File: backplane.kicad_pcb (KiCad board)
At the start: 4 copper layers, 110 x 90 mm, 55 parts, among them J0 212520-1006, J1 SFMC-110-01-L-D, J2 SFMC-110-01-L-D, J3 SFMC-110-01-L-D, J5 XT60PW-F, Q1 SSM3K15AMFV,L3F, U1 SiC437BED-T1-GE3

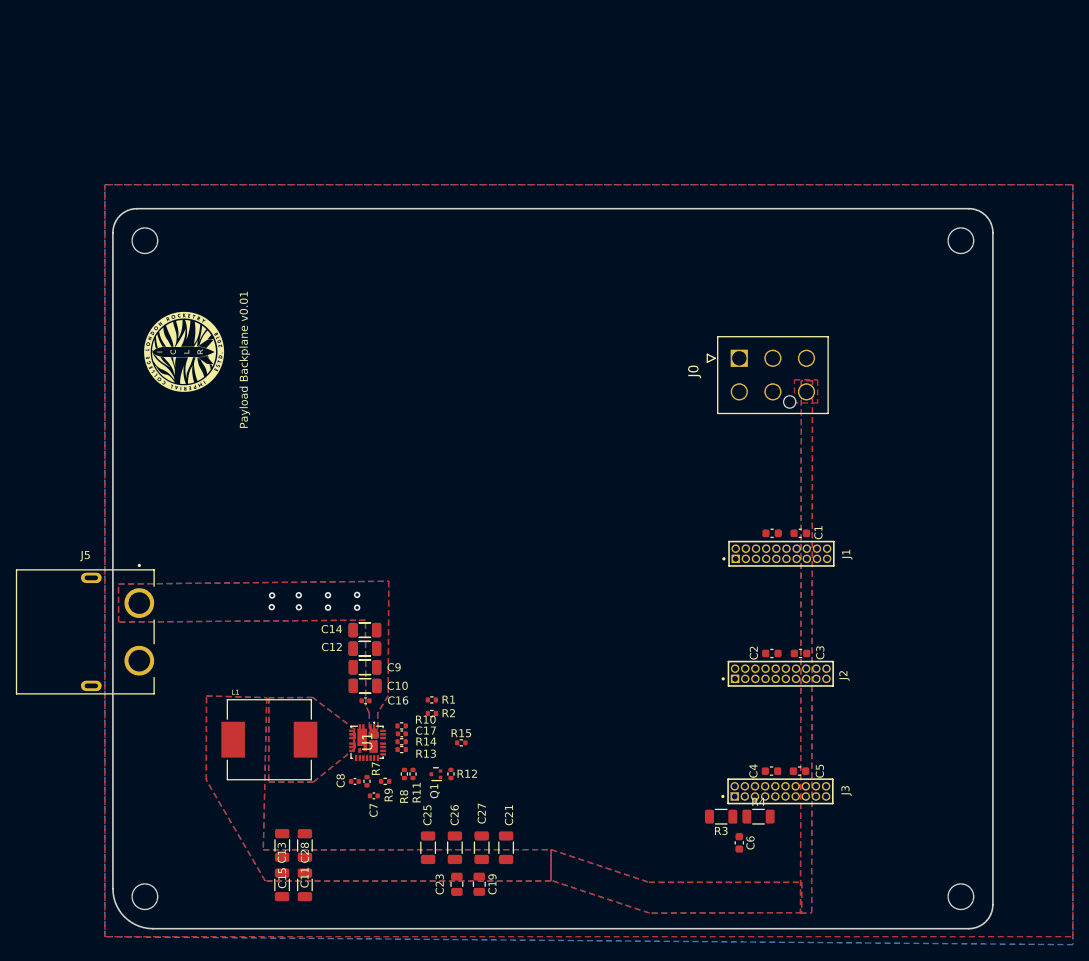
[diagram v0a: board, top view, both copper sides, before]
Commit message: Overhaul of design
Changed out the SFMC Oresat connectors for the 46010-0622 Molex; added the SC4215; reduced from 4 connectors to three connectors - no changes made to the footprint, changes only made to the schematic for checks
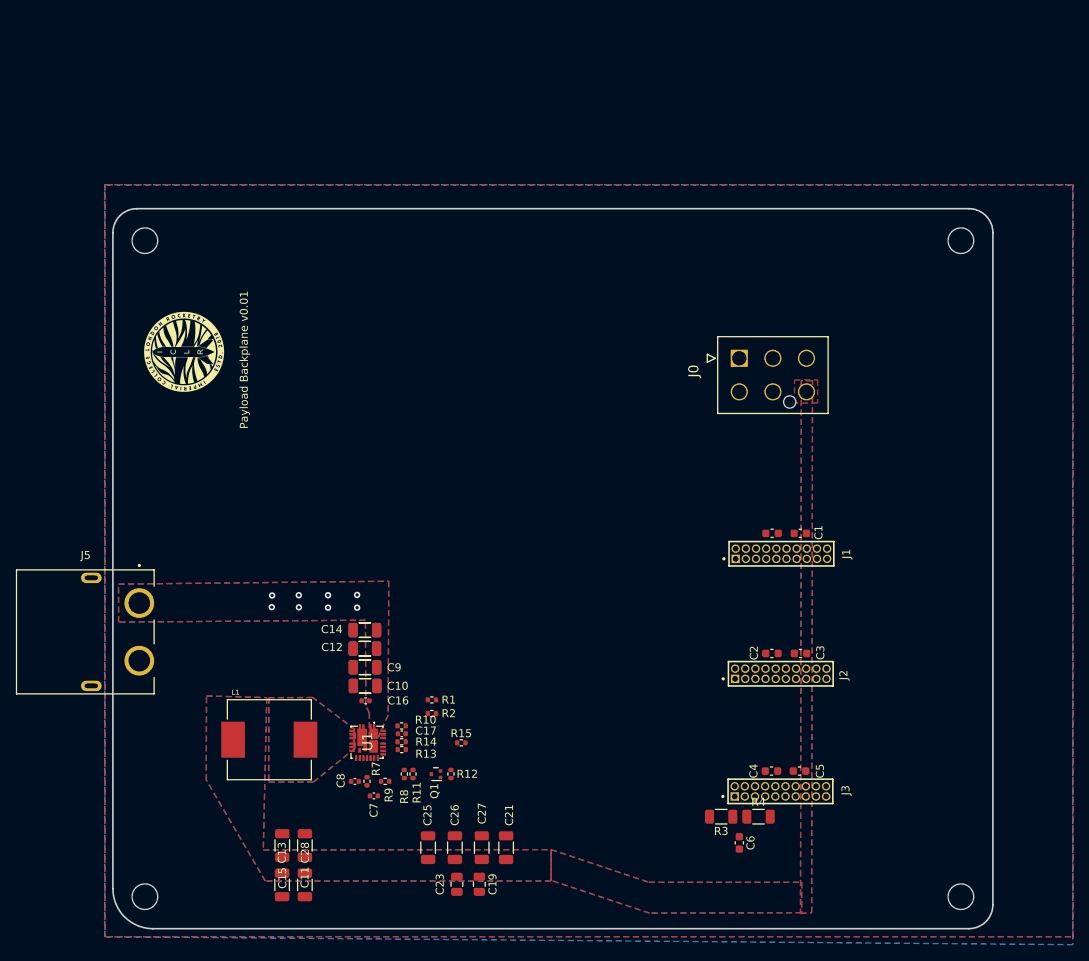
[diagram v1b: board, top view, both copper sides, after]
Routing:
- added copper zone on In2.Cu, net +3.3V
- removed copper zone on In2.Cu, net GND
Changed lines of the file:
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@@
   (via (at 113.89 106.32) (size 0.8) (drill 0.4) (layers "F.Cu" "B.Cu") (free) (net 11))
   (via (at 113.89 107.87) (size 0.8) (drill 0.4) (layers "F.Cu" "B.Cu") (free) (net 11))
-  (zone (net 2) (net_name "GND") (layer "F.Cu") (hatch edge 0.5)
+  (zone (net 0) (net_name "") (layer "F.Cu") (hatch edge 0.5)
+    (priority 6)
+    (connect_pads (clearance 0.254))
+    (min_thickness 0.25) (filled_areas_thickness no)
+    (fill yes (thermal_gap 0.5) (thermal_bridge_width 0.5) (island_removal_mode 1) (island_area_min 10))
+    (polygon
+      (pts
+        (xy 172.2 79.4)
+        (xy 175.1 79.4)
+        (xy 175.1 82.3)
+        (xy 172.2 82.3)
+      )
+    )
+  )
+  (zone (net 2) (net_name "GND") (layers "F.Cu" "In1.Cu" "B.Cu") (hatch edge 0.5)
     (priority 1)
-    (connect_pads (clearance 0.5))
+    (connect_pads yes (clearance 0.5))
     (min_thickness 0.25) (filled_areas_thickness no)
     (fill yes (thermal_gap 0.5) (thermal_bridge_width 0.5))
@@
         (xy 86 55)
         (xy 86 149)
-      )
-    )
-  )
-  (zone (net 0) (net_name "") (layer "F.Cu") (hatch edge 0.5)
-    (priority 6)
-    (connect_pads (clearance 0.254))
-    (min_thickness 0.25) (filled_areas_thickness no)
-    (fill (thermal_gap 0.5) (thermal_bridge_width 0.5) (island_removal_mode 1) (island_area_min 10))
-    (polygon
-      (pts
-        (xy 172.2 79.4)
-        (xy 175.1 79.4)
-        (xy 175.1 82.3)
-        (xy 172.2 82.3)
       )
     )
@@
         (xy 121.48 104.57)
         (xy 121.42 118.89)
-        (xy 120.1 121.01)
+        (xy 121.4 121.3)
         (xy 120.13 124.16)
       )
@@
     (connect_pads yes (clearance 0.254))
     (min_thickness 0.25) (filled_areas_thickness no)
-    (fill (thermal_gap 0.5) (thermal_bridge_width 0.5))
+    (fill yes (thermal_gap 0.5) (thermal_bridge_width 0.5))
     (polygon
       (pts
@@
     )
   )
-  (zone (net 2) (net_name "GND") (layer "In2.Cu") (hatch edge 0.5)
-    (priority 3)
-    (connect_pads (clearance 0.5))
+  (zone (net 12) (net_name "+3.3V") (layer "In2.Cu") (hatch edge 0.5)
+    (priority 1)
+    (connect_pads yes (clearance 0.5))
     (min_thickness 0.25) (filled_areas_thickness no)
     (fill yes (thermal_gap 0.5) (thermal_bridge_width 0.5))

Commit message: Configuring stuff
wires and zones added - will change to Si438 + add a switch at some point + some mistakes to still iron out
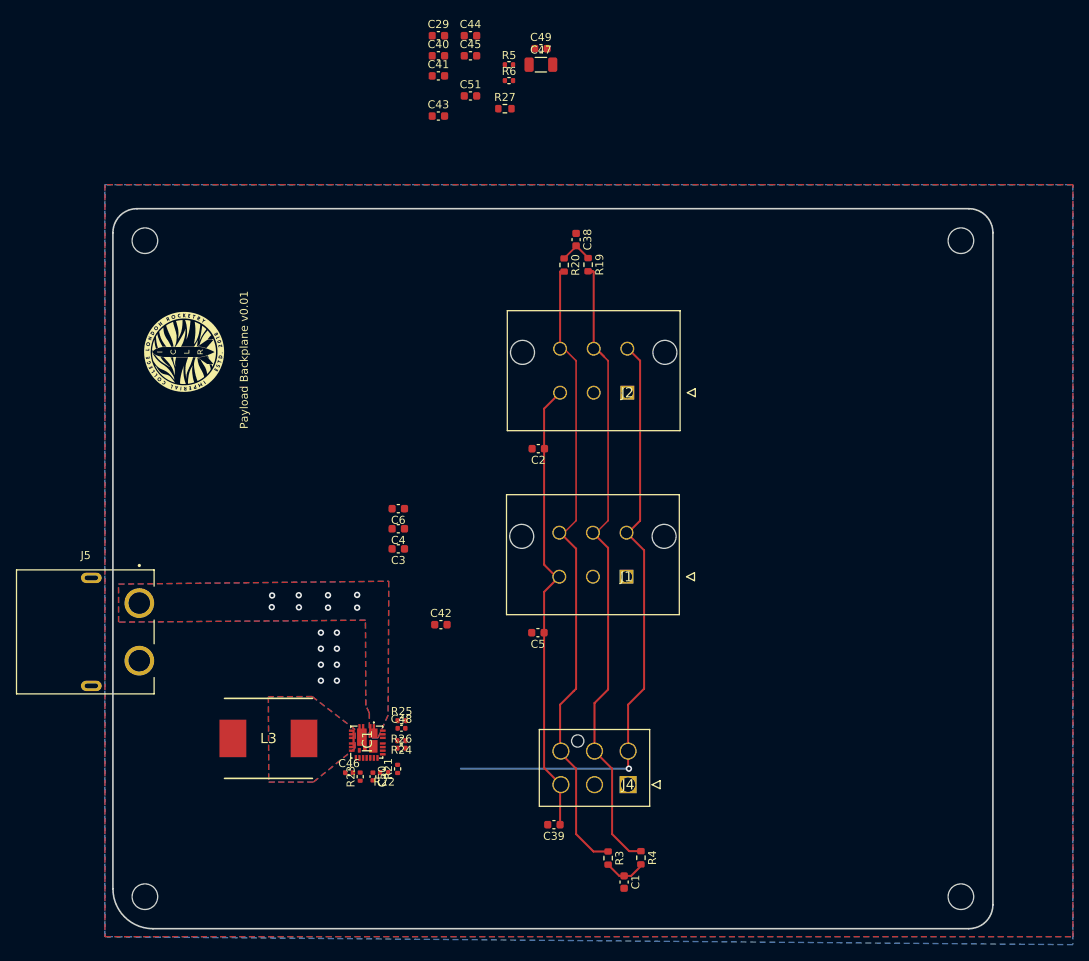
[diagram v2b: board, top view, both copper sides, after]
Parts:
- removed C10, C11, C13, C15, C28, C9: 47uF, Capacitor_SMD:C_1206_3216Metric
- removed C12, C14, C18, C20, C21, C22, C24, C25, C26, C27: DNP, Capacitor_SMD:C_1206_3216Metric
- removed C16: 100nF, Capacitor_SMD:C_0402_1005Metric
- removed C17: 0.1uF, Capacitor_SMD:C_0402_1005Metric
- removed C19, C23: DNP, Capacitor_SMD:C_0805_2012Metric
- removed C7: 1uF, Capacitor_SMD:C_0402_1005Metric
- removed C8: 4.7uF, Capacitor_SMD:C_0402_1005Metric
- removed J0: 212520-1006, Molex 212520-1006:212520-1006
- removed J3: SFMC-110-01-L-D, SFMC-110-01-L-D:SAMTEC_SFMC-110-01-L-D
- removed L1: 1.5uH, SPM10065VT_3R3M_D:IND_SPM10065VT-3R3M-D
- removed Q1: SSM3K15AMFV,L3F, Package_TO_SOT_SMD:SOT-723
- removed R1: 1.5k, Resistor_SMD:R_0402_1005Metric
- removed R10: 2.2, Resistor_SMD:R_0402_1005Metric
- removed R11, R8: 90k, Resistor_SMD:R_0402_1005Metric
- removed R12: 1k, Resistor_SMD:R_0402_1005Metric
- removed R13: 200k, Resistor_SMD:R_0402_1005Metric
- removed R14: 100k, Resistor_SMD:R_0402_1005Metric
- removed R15, R7, R9: 10k, Resistor_SMD:R_0402_1005Metric
- removed R2: 2.2k, Resistor_SMD:R_0402_1005Metric
- removed U1: SiC437BED-T1-GE3, iclr:SiC437BEDT1GE3
- added C38: C_Small, Capacitor_SMD:C_0603_1608Metric, F.Cu at (144.9, 61.9)
- added C39: C_Small, Capacitor_SMD:C_0603_1608Metric, F.Cu at (142.1, 135.0)
- added C40: 22uF, Capacitor_SMD:C_0603_1608Metric, F.Cu at (127.7, 38.9)
- added C41: 22uF, Capacitor_SMD:C_0603_1608Metric, F.Cu at (127.7, 41.4)
- added C42: 22uF, Capacitor_SMD:C_0603_1608Metric, F.Cu at (128.0, 110.0)
- added C43: 22uF, Capacitor_SMD:C_0603_1608Metric, F.Cu at (127.7, 46.4)
- added C44: 22uF, Capacitor_SMD:C_0603_1608Metric, F.Cu at (131.7, 36.4)
- added C45: 22uF, Capacitor_SMD:C_0603_1608Metric, F.Cu at (131.7, 38.9)
- added C46: 4.7uF, Capacitor_SMD:C_0402_1005Metric, F.Cu at (116.5, 128.5)
- added C47: 47uF, Capacitor_SMD:C_1206_3216Metric, F.Cu at (140.5, 40.0)
- added C48: 0.1uF, Capacitor_SMD:C_0402_1005Metric, F.Cu at (123.1, 123.0)
- added C49: 100nF, Capacitor_SMD:C_0603_1608Metric, F.Cu at (140.5, 38.0)
- added C50: 1uF, Capacitor_SMD:C_0402_1005Metric, F.Cu at (119.5, 129.0)
- added C51: 680pF, Capacitor_SMD:C_0603_1608Metric, F.Cu at (131.7, 43.9)
- added IC1: SiC437AED-T1-GE3, iclr:SiC437BEDT1GE3, F.Cu at (118.7, 124.7)
- added J4: 212520-1006, iclr:212520-1006, F.Cu at (151.4, 130.0)
- added L3: SRP1050WA-3R3M, iclr:INDPM110100X540N, F.Cu at (106.4, 124.2)
- added R19: 60.4, Resistor_SMD:R_0603_1608Metric, F.Cu at (146.4, 65.0)
- added R20: 60.4, Resistor_SMD:R_0603_1608Metric, F.Cu at (143.4, 65.0)
- added R21: 45k, Resistor_SMD:R_0402_1005Metric, F.Cu at (122.6, 128.0)
- added R22: 10k, Resistor_SMD:R_0402_1005Metric, F.Cu at (120.9, 128.5)
- added R23: 10k, Resistor_SMD:R_0402_1005Metric, F.Cu at (117.9, 129.0)
- added R24: 51k, Resistor_SMD:R_0402_1005Metric, F.Cu at (123.1, 124.5)
- added R25: 2.2, Resistor_SMD:R_0402_1005Metric, F.Cu at (123.1, 122.0)
- added R26: 100k, Resistor_SMD:R_0402_1005Metric, F.Cu at (123.1, 125.4)
- added R27: 5.1, Resistor_SMD:R_0603_1608Metric, F.Cu at (136.0, 45.5)
- added R5: 10k, Resistor_SMD:R_0402_1005Metric, F.Cu at (136.5, 40.0)
- added R6: 160k, Resistor_SMD:R_0402_1005Metric, F.Cu at (136.5, 42.0)
- C1, C2, C3, C4, C5: value C -> C_Small
- C29: value C -> 22uF
- C6: value 1n -> C_Small
- J1, J2: value SFMC-110-01-L-D -> 46010-0622; footprint SFMC-110-01-L-D:SAMTEC_SFMC-110-01-L-D -> iclr:46010-06YY
- R3, R4: footprint Resistor_SMD:R_1206_3216Metric -> Resistor_SMD:R_0603_1608Metric
- moved C29 74.9 mm to (127.7, 36.4)
- moved C6 59.7 mm to (122.7, 95.5), turned to 180 degrees
- moved C4 55.6 mm to (122.7, 98.0), turned to 180 degrees
- moved C3 52.0 mm to (122.7, 100.5), turned to 180 degrees
- moved C1 48.8 mm to (150.9, 142.2), turned to -90 degrees
- moved C2 38.8 mm to (140.2, 88.0), turned to 180 degrees
- moved J2 38.2 mm to (151.3, 81.0)
- moved C5 37.0 mm to (140.1, 111.0), turned to 180 degrees
- moved R4 15.6 mm to (153.0, 139.1), turned to -90 degrees
- moved R3 15.1 mm to (148.9, 139.2), turned to -90 degrees
- moved J1 13.8 mm to (151.2, 104.0)
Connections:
- C1 pad 1: GND -> Net-(C1-Pad1)
- C1 pad 2: 3.3VBUS -> GND
- C2 pad 1: 12V -> +3.3V
- C29 pad 1: 12V -> GND
- C29 pad 2: GND -> RBUS_uC_V
- C3 pad 2: 3.3VBUS -> +12V
- C4 pad 1: 12V -> GND
- C4 pad 2: GND -> +12V
- C5 pad 1: GND -> +3.3V
- C5 pad 2: 3.3VBUS -> GND
- C6 pad 1: Net-(C6-Pad1) -> GND
- C6 pad 2: GND -> +12V
- J5 pad 2: GND -> /GND
- J5 pad S1: GND -> /GND
- J5 pad S2: GND -> /GND
- R3 pad 2: Net-(C6-Pad1) -> Net-(C1-Pad1)
- R4 pad 2: Net-(C6-Pad1) -> Net-(C1-Pad1)
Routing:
- net CAN_L: track 0.00 -> 81.2 mm
- net CAN_H: track 0.25 -> 80.6 mm
- net +12V: track 0.00 -> 76.8 mm, vias 8 -> 9
- net +3.3V: track 0.00 -> 57.4 mm
- net Net-(C1-Pad1): track 0.00 -> 5.49 mm
- net Net-(C38-Pad2): track 0.00 -> 4.35 mm
- net GND: track 0.00 -> 0.50 mm, vias 0 -> 8
- removed copper zone on F.Cu, net (none)

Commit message: neatened things
leds
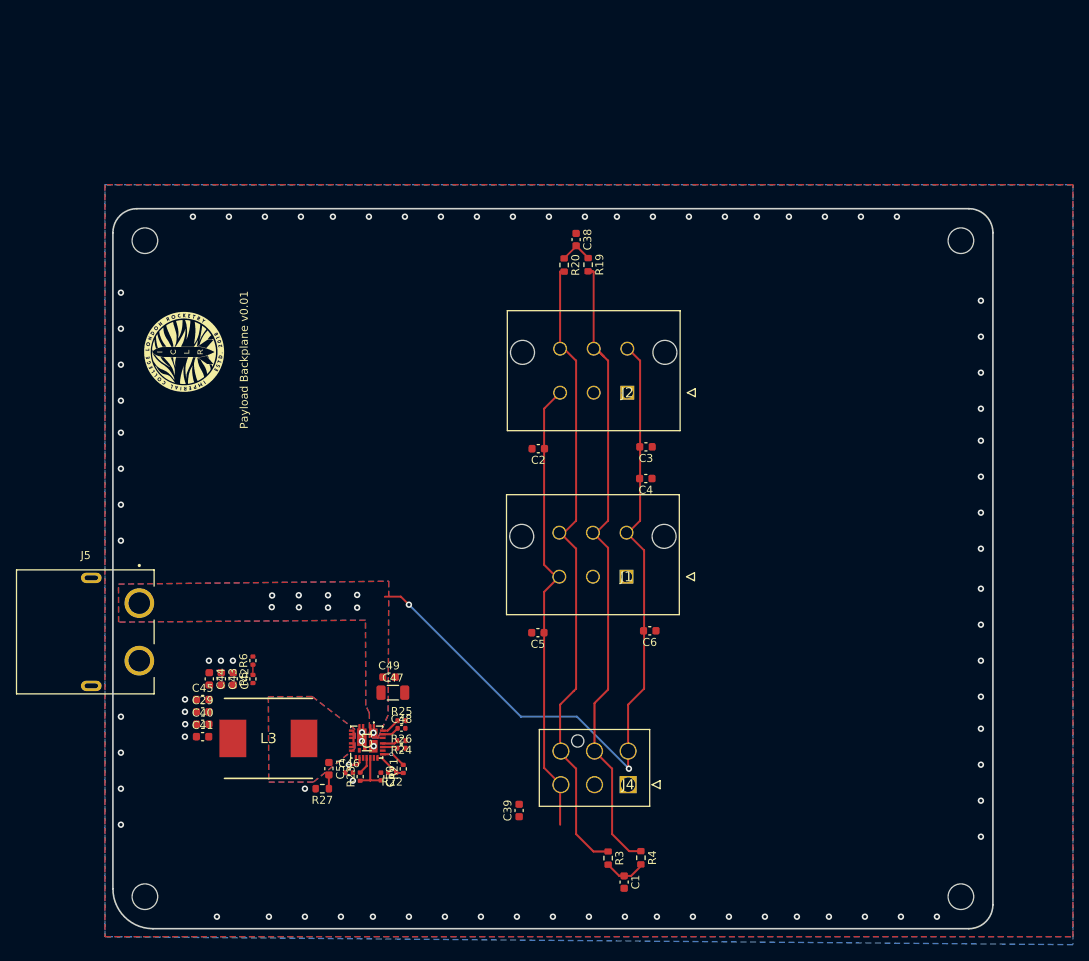
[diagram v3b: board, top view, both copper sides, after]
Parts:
- moved C29 89.5 mm to (98.2, 120.9)
- moved C40 88.6 mm to (98.2, 122.5)
- moved R27 88.0 mm to (113.2, 130.5), turned to 180 degrees
- moved C41 87.7 mm to (98.2, 124.0)
- moved C45 87.1 mm to (98.2, 119.3)
- moved C44 86.8 mm to (99.0, 116.8), turned to -90 degrees
- moved C51 85.9 mm to (114.0, 128.0), turned to -90 degrees
- moved R5 83.2 mm to (104.5, 116.8), turned to 90 degrees
- moved C49 80.8 mm to (121.5, 116.6)
- moved C47 80.7 mm to (122.0, 118.5)
- moved R6 79.3 mm to (104.5, 114.5), turned to 90 degrees
- moved C43 75.4 mm to (100.5, 116.8), turned to -90 degrees
- moved C6 34.9 mm to (154.1, 110.8)
- moved C3 33.5 mm to (153.6, 87.8)
- moved C4 31.6 mm to (153.6, 91.7)
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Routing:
- net +12V: track 76.8 -> 95.5 mm, vias 9 -> 10
- net /buckC/Vdd: track 0.00 -> 5.41 mm
- net /buckC/FB: track 0.00 -> 4.00 mm
- net Net-(IC1-V_DRV): track 0.00 -> 3.22 mm, vias 0 -> 1
- net RBUS_uC_V: track 0.00 -> 3.11 mm, vias 0 -> 1
- net /buckC/PHASE: track 0.00 -> 2.37 mm
- net /buckC/BOOT: track 0.00 -> 2.16 mm
- net Net-(IC1-P_GOOD): track 0.00 -> 2.16 mm
- net /buckC/MODE_1: track 0.00 -> 1.96 mm
- net /buckC/MODE_2: track 0.00 -> 1.88 mm
- net Net-(C51-Pad2): track 0.00 -> 1.72 mm
- net Net-(IC1-EN): track 0.00 -> 1.59 mm, vias 0 -> 1
- net Net-(R5-Pad2): track 0.00 -> 1.27 mm
- net GND: vias 8 -> 82
